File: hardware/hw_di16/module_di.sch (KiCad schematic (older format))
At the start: 142 parts, among them P1 DEBUG, P2 DI_0, P3 DI_1, P4 MOD_IN, U1 STM32F103C8Tx, U2 TLP291-4, U3 TLP291-4, U4 TLP291-4, U5 TLP291-4

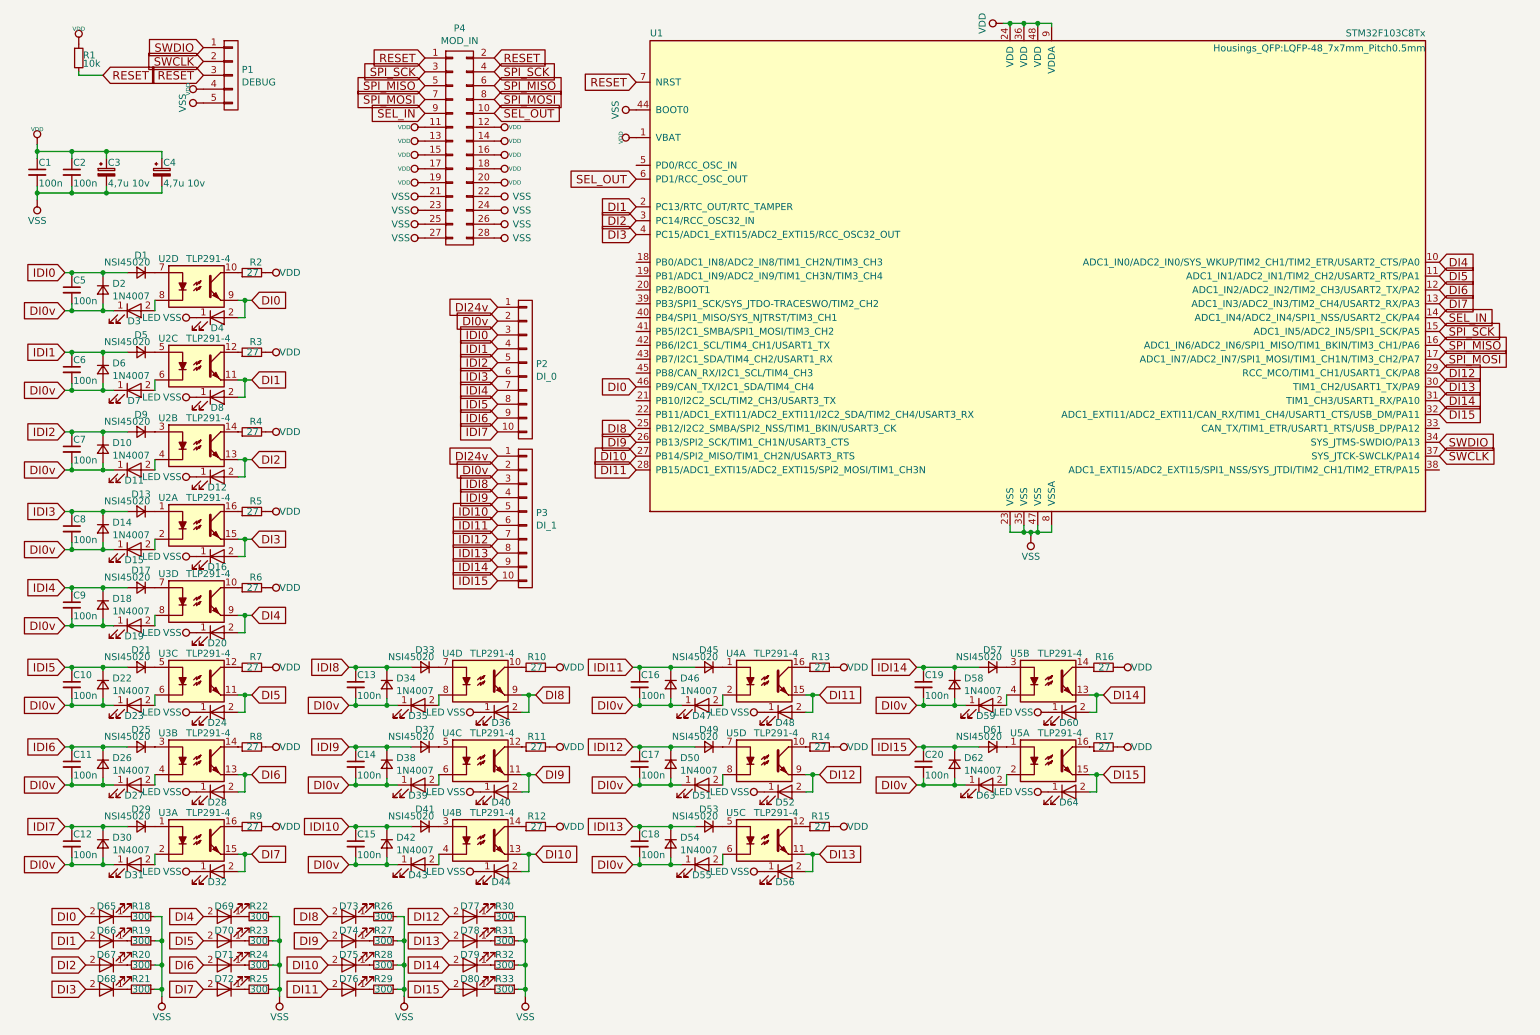
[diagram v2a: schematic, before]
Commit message: Обновлена плата DI16.
Завершена предварительная разводка.
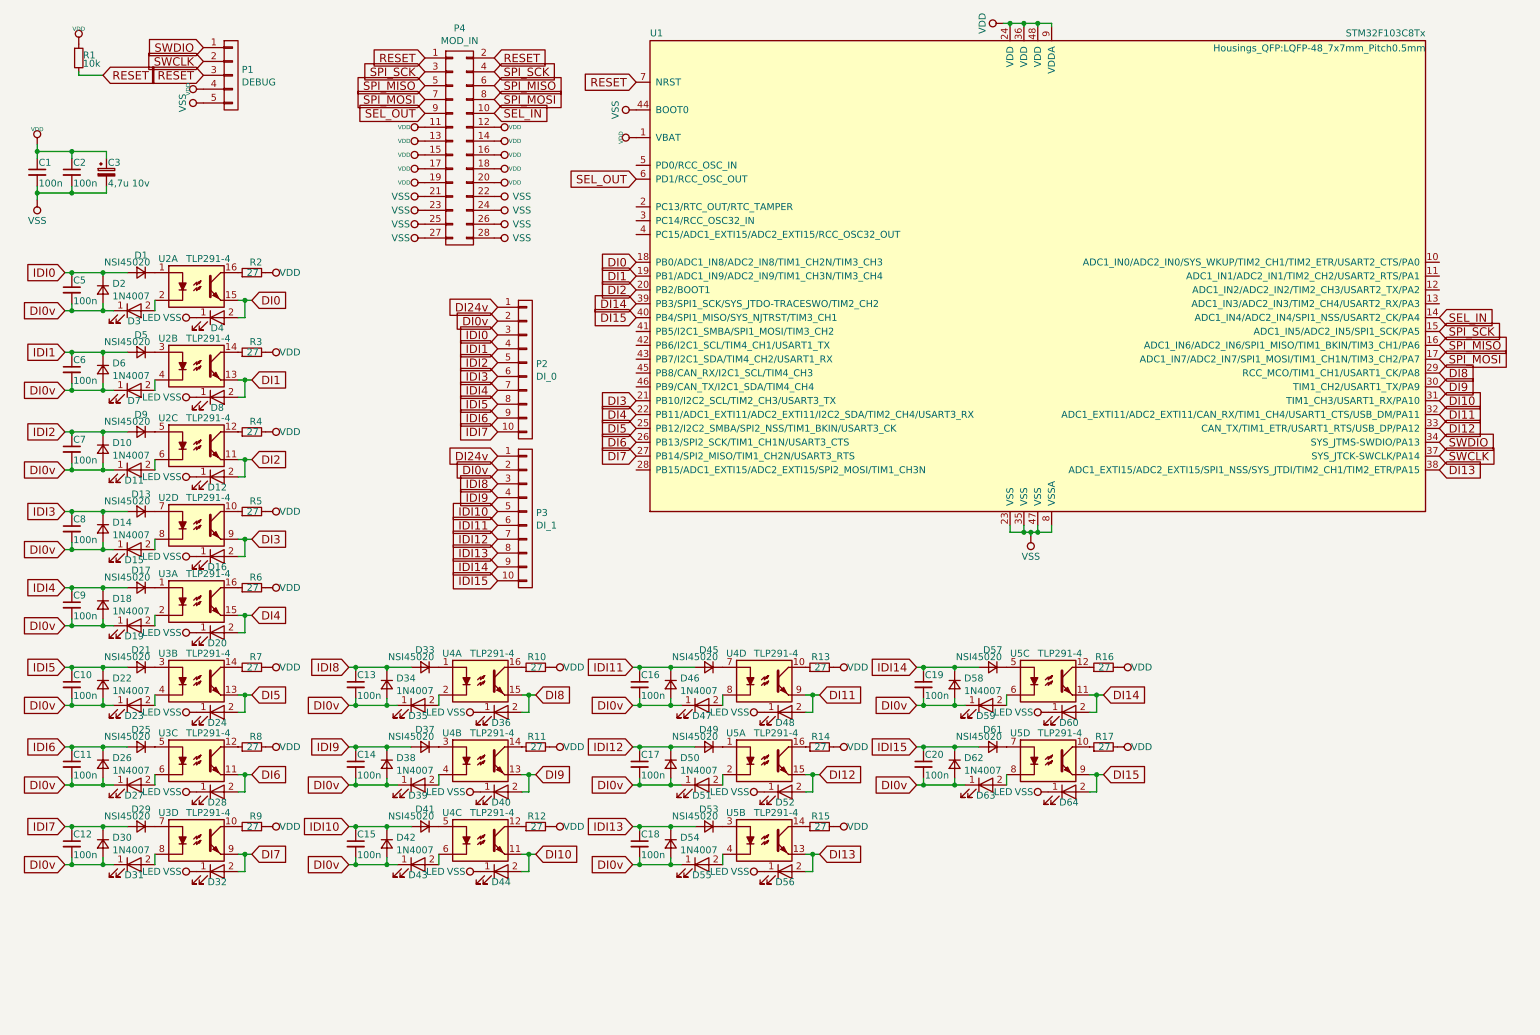
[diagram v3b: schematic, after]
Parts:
- removed C4: 4,7u 10v, Capacitors_Tantalum_SMD:CP_Tantalum_Case-A_EIA-3216-18_Reflow, symbol CP_Small
- removed D65, D66, D67, D68, D69, D70, D71, D72, D73, D74, D75, D76, D77, D78, D79, D80: LED, LEDs:LED_0805, symbol LED
- removed R18, R19, R20, R21, R22, R23, R24, R25, R26, R27, R28, R29, R30, R31, R32, R33: 300, Resistors_SMD:R_0805, symbol R_Small
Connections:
- net DI0: now also U1.18 (PB0/ADC1_IN8/ADC2_IN8/TIM1_CH2N/TIM3_CH3), U2.15; no longer U1.46 (PB9/CAN_TX/I2C1_SDA/TIM4_CH4), U2.9
- net DI1: now also U1.19 (PB1/ADC1_IN9/ADC2_IN9/TIM1_CH3N/TIM3_CH4), U2.13; no longer U1.2 (PC13/RTC_OUT/RTC_TAMPER), U2.11
- net DI10: now also U1.31 (TIM1_CH3/USART1_RX/PA10), U4.11; no longer U1.27 (PB14/SPI2_MISO/TIM1_CH2N/USART3_RTS), U4.13
- net DI11: now also U1.32 (ADC1_EXTI11/ADC2_EXTI11/CAN_RX/TIM1_CH4/USART1_CTS/USB_DM/PA11), U4.9; no longer U1.28 (PB15/ADC1_EXTI15/ADC2_EXTI15/SPI2_MOSI/TIM1_CH3N), U4.15
- net DI12: now also U1.33 (CAN_TX/TIM1_ETR/USART1_RTS/USB_DP/PA12), U5.15; no longer U1.29 (RCC_MCO/TIM1_CH1/USART1_CK/PA8), U5.9
- net DI13: now also U1.38 (ADC1_EXTI15/ADC2_EXTI15/SPI1_NSS/SYS_JTDI/TIM2_CH1/TIM2_ETR/PA15), U5.13; no longer U1.30 (TIM1_CH2/USART1_TX/PA9), U5.11
- net DI14: now also U1.39 (PB3/SPI1_SCK/SYS_JTDO-TRACESWO/TIM2_CH2), U5.11; no longer U1.31 (TIM1_CH3/USART1_RX/PA10), U5.13
- net DI15: now also U1.40 (PB4/SPI1_MISO/SYS_NJTRST/TIM3_CH1), U5.9; no longer U1.32 (ADC1_EXTI11/ADC2_EXTI11/CAN_RX/TIM1_CH4/USART1_CTS/USB_DM/PA11), U5.15
- net DI2: now also U1.20 (PB2/BOOT1), U2.11; no longer U1.3 (PC14/RCC_OSC32_IN), U2.13
- net DI3: now also U1.21 (PB10/I2C2_SCL/TIM2_CH3/USART3_TX), U2.9; no longer U1.4 (PC15/ADC1_EXTI15/ADC2_EXTI15/RCC_OSC32_OUT), U2.15
- net DI4: now also U1.22 (PB11/ADC1_EXTI11/ADC2_EXTI11/I2C2_SDA/TIM2_CH4/USART3_RX), U3.15; no longer U1.10 (ADC1_IN0/ADC2_IN0/SYS_WKUP/TIM2_CH1/TIM2_ETR/USART2_CTS/PA0), U3.9
- net DI5: now also U1.25 (PB12/I2C2_SMBA/SPI2_NSS/TIM1_BKIN/USART3_CK), U3.13; no longer U1.11 (ADC1_IN1/ADC2_IN1/TIM2_CH2/USART2_RTS/PA1), U3.11
- net DI6: now also U1.26 (PB13/SPI2_SCK/TIM1_CH1N/USART3_CTS), U3.11; no longer U1.12 (ADC1_IN2/ADC2_IN2/TIM2_CH3/USART2_TX/PA2), U3.13
- net DI7: now also U1.27 (PB14/SPI2_MISO/TIM1_CH2N/USART3_RTS), U3.9; no longer U1.13 (ADC1_IN3/ADC2_IN3/TIM2_CH4/USART2_RX/PA3), U3.15
- net DI8: now also U1.29 (RCC_MCO/TIM1_CH1/USART1_CK/PA8), U4.15; no longer U1.25 (PB12/I2C2_SMBA/SPI2_NSS/TIM1_BKIN/USART3_CK), U4.9
- net DI9: now also U1.30 (TIM1_CH2/USART1_TX/PA9), U4.13; no longer U1.26 (PB13/SPI2_SCK/TIM1_CH1N/USART3_CTS), U4.11
- net SEL_IN: now also P4.10 (P10); no longer P4.9 (P9)
- net SEL_OUT: now also P4.9 (P9); no longer P4.10 (P10)
- net at R2.1: now also U2.16; no longer U2.10
- net at D1.1 (K): now also U2.1; no longer U2.7
- net at D3.2 (A): now also U2.2; no longer U2.8
- net at R3.1: now also U2.14; no longer U2.12
- net at D5.1 (K): now also U2.3; no longer U2.5
- net at D7.2 (A): now also U2.4; no longer U2.6
- net at R4.1: now also U2.12; no longer U2.14
- net at D9.1 (K): now also U2.5; no longer U2.3
- net at D11.2 (A): now also U2.6; no longer U2.4
- net at D13.1 (K): now also U2.7; no longer U2.1
- net at R5.1: now also U2.10; no longer U2.16
- net at D15.2 (A): now also U2.8; no longer U2.2
- net at R6.1: now also U3.16; no longer U3.10
- net at D17.1 (K): now also U3.1; no longer U3.7
- net at D19.2 (A): now also U3.2; no longer U3.8
- net at R7.1: now also U3.14; no longer U3.12
- net at D21.1 (K): now also U3.3; no longer U3.5
- net at D23.2 (A): now also U3.4; no longer U3.6
- net at R8.1: now also U3.12; no longer U3.14
- net at D25.1 (K): now also U3.5; no longer U3.3
- net at D27.2 (A): now also U3.6; no longer U3.4
- net at D29.1 (K): now also U3.7; no longer U3.1
- net at R9.1: now also U3.10; no longer U3.16
- net at D31.2 (A): now also U3.8; no longer U3.2
- net at R10.1: now also U4.16; no longer U4.10
- net at D33.1 (K): now also U4.1; no longer U4.7
- net at D35.2 (A): now also U4.2; no longer U4.8
- net at R11.1: now also U4.14; no longer U4.12
- net at D37.1 (K): now also U4.3; no longer U4.5
- net at D39.2 (A): now also U4.4; no longer U4.6
- net at R12.1: now also U4.12; no longer U4.14
- net at D41.1 (K): now also U4.5; no longer U4.3
- net at D43.2 (A): now also U4.6; no longer U4.4
- net at D45.1 (K): now also U4.7; no longer U4.1
- net at R13.1: now also U4.10; no longer U4.16
- net at D47.2 (A): now also U4.8; no longer U4.2
- net at R14.1: now also U5.16; no longer U5.10
- net at D49.1 (K): now also U5.1; no longer U5.7
- net at D51.2 (A): now also U5.2; no longer U5.8
- net at R15.1: now also U5.14; no longer U5.12
- net at D53.1 (K): now also U5.3; no longer U5.5
- net at D55.2 (A): now also U5.4; no longer U5.6
- net at R16.1: now also U5.12; no longer U5.14
- net at D57.1 (K): now also U5.5; no longer U5.3
- net at D59.2 (A): now also U5.6; no longer U5.4
- net at D61.1 (K): now also U5.7; no longer U5.1
- net at R17.1: now also U5.10; no longer U5.16
- net at D63.2 (A): now also U5.8; no longer U5.2

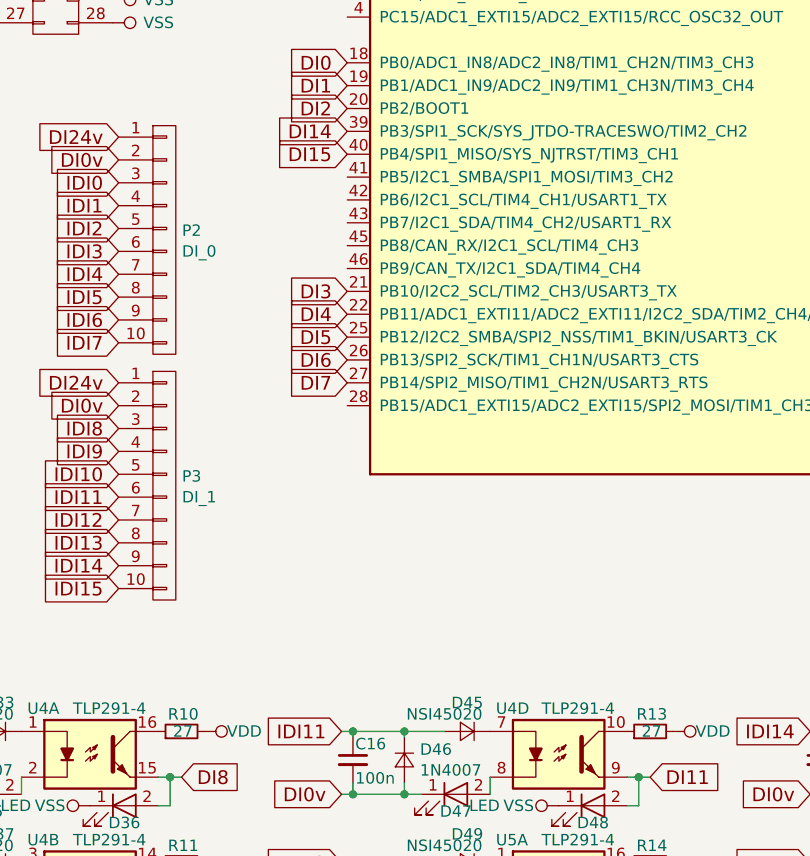
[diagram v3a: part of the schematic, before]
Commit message: Обновлена плата модуля DI16.
Добавлены статусные светодиоды.
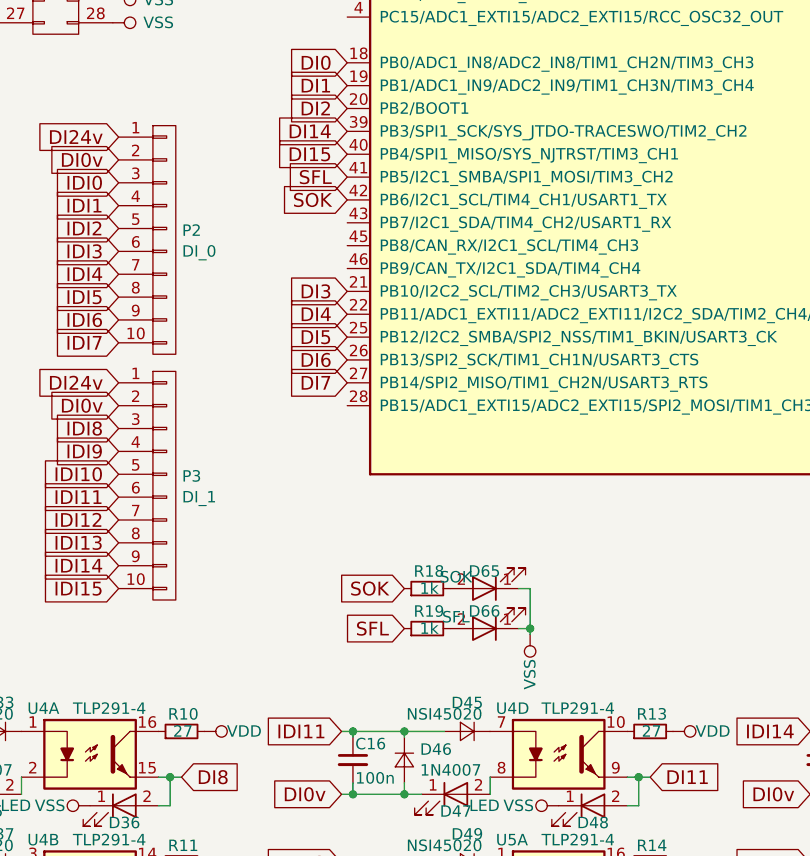
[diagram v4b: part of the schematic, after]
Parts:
- added D65: SOK, LEDs:LED_0805, symbol LED
- added D66: SFL, LEDs:LED_0805, symbol LED
- added R18, R19: 1k, Resistors_SMD:R_0805, symbol R_Small
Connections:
- net VSS: now also D65.1 (K), D66.1 (K)
- net SFL: now reaches U1.41 (PB5/I2C1_SMBA/SPI1_MOSI/TIM3_CH2)
- net SFL: now also R19.1
- net SOK: now reaches U1.42 (PB6/I2C1_SCL/TIM4_CH1/USART1_TX)
- net SOK: now also R18.1
- new net: D65.2 (A), R18.2
- new net: D66.2 (A), R19.2

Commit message: Обновлена шелкография на платах.
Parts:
- D11, D12, D15, D16, D19, D20, D23, D24, D27, D28, D3, D31, D32, D35, D36, D39, D4, D40, D43, D44, D47, D48, D51, D52, D55, D56, D59, D60, D63, D64, D65, D66, D7, D8: footprint LEDs:LED_0805 -> LEDs:LED_0603

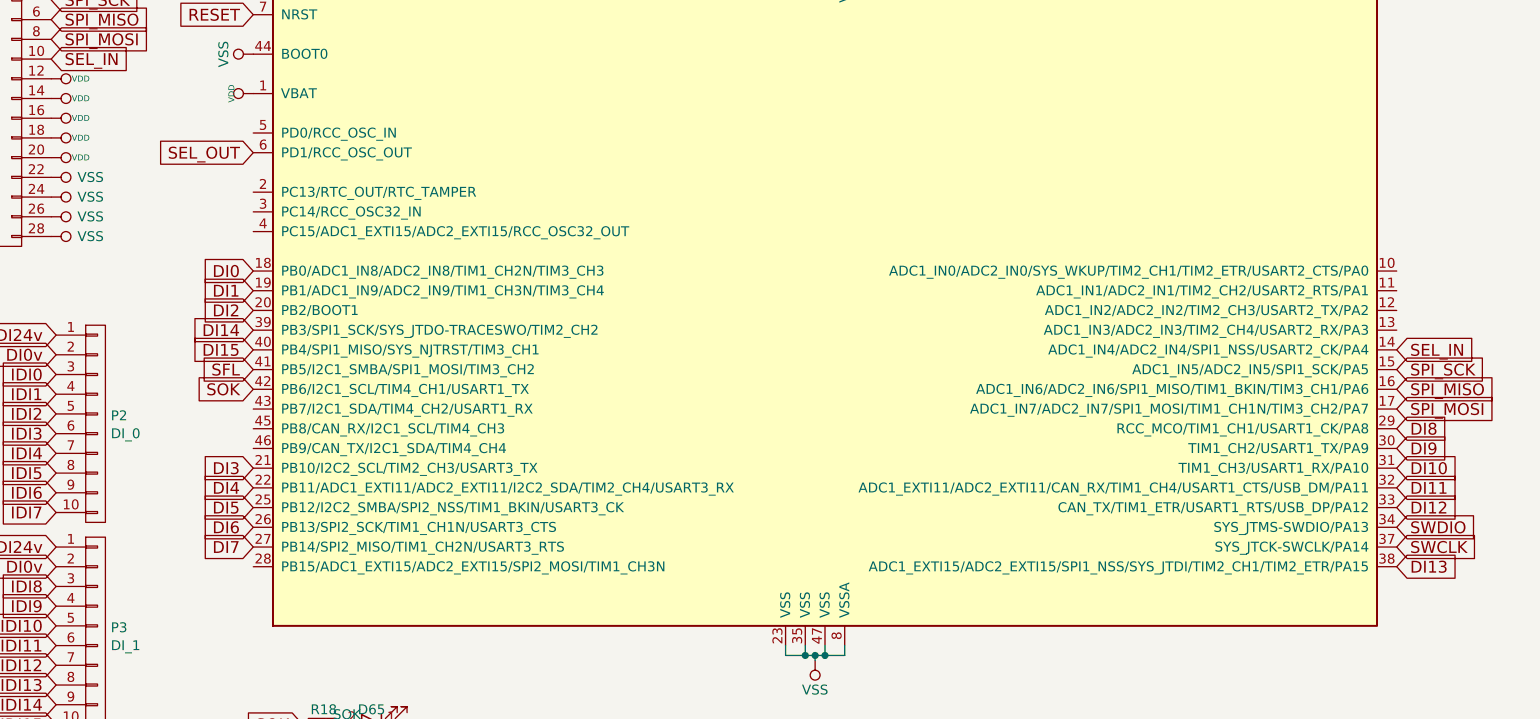
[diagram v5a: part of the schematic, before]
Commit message: Обновлены платы модулей - приведены к единому виду.
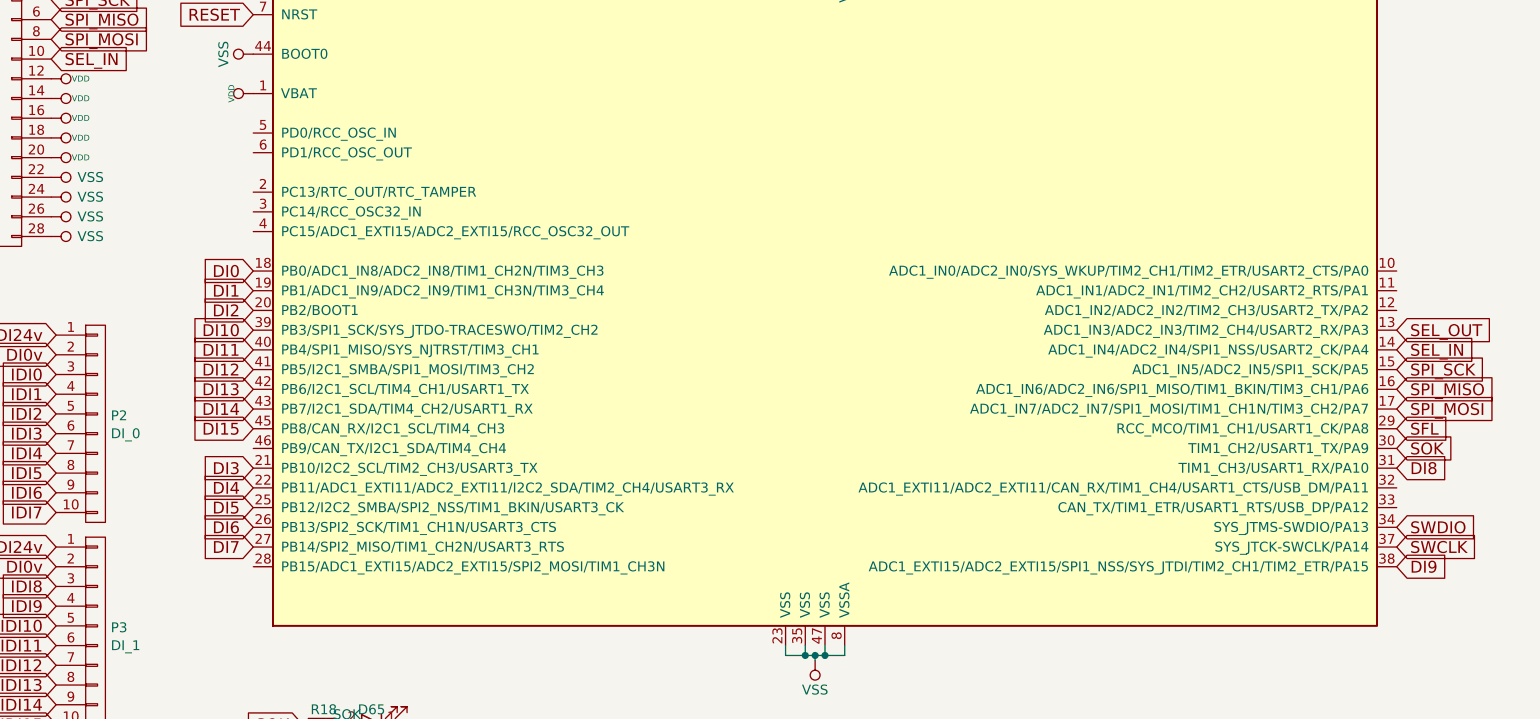
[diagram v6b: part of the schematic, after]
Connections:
- net DI10: now also U1.39 (PB3/SPI1_SCK/SYS_JTDO-TRACESWO/TIM2_CH2); no longer U1.31 (TIM1_CH3/USART1_RX/PA10)
- net DI11: now also U1.40 (PB4/SPI1_MISO/SYS_NJTRST/TIM3_CH1); no longer U1.32 (ADC1_EXTI11/ADC2_EXTI11/CAN_RX/TIM1_CH4/USART1_CTS/USB_DM/PA11)
- net DI12: now also U1.41 (PB5/I2C1_SMBA/SPI1_MOSI/TIM3_CH2); no longer U1.33 (CAN_TX/TIM1_ETR/USART1_RTS/USB_DP/PA12)
- net DI13: now also U1.42 (PB6/I2C1_SCL/TIM4_CH1/USART1_TX); no longer U1.38 (ADC1_EXTI15/ADC2_EXTI15/SPI1_NSS/SYS_JTDI/TIM2_CH1/TIM2_ETR/PA15)
- net DI14: now also U1.43 (PB7/I2C1_SDA/TIM4_CH2/USART1_RX); no longer U1.39 (PB3/SPI1_SCK/SYS_JTDO-TRACESWO/TIM2_CH2)
- net DI15: now also U1.45 (PB8/CAN_RX/I2C1_SCL/TIM4_CH3); no longer U1.40 (PB4/SPI1_MISO/SYS_NJTRST/TIM3_CH1)
- net DI8: now also U1.31 (TIM1_CH3/USART1_RX/PA10); no longer U1.29 (RCC_MCO/TIM1_CH1/USART1_CK/PA8)
- net DI9: now also U1.38 (ADC1_EXTI15/ADC2_EXTI15/SPI1_NSS/SYS_JTDI/TIM2_CH1/TIM2_ETR/PA15); no longer U1.30 (TIM1_CH2/USART1_TX/PA9)
- net SEL_OUT: now also U1.13 (ADC1_IN3/ADC2_IN3/TIM2_CH4/USART2_RX/PA3); no longer U1.6 (PD1/RCC_OSC_OUT)
- net SFL: now also U1.29 (RCC_MCO/TIM1_CH1/USART1_CK/PA8); no longer U1.41 (PB5/I2C1_SMBA/SPI1_MOSI/TIM3_CH2)
- net SOK: now also U1.30 (TIM1_CH2/USART1_TX/PA9); no longer U1.42 (PB6/I2C1_SCL/TIM4_CH1/USART1_TX)
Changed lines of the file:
@@
 LIBS:powerint
 LIBS:module_di-cache
-EELAYER 25 0
+EELAYER 26 0
 EELAYER END
 $Descr A4 11693 8268
@@
 Comment4 ""
 $EndDescr
-Text GLabel 4925 2650 0    60   Input ~ 0
+Text GLabel 4925 3050 0    60   Input ~ 0
 DI15
-Text GLabel 4925 2550 0    60   Input ~ 0
+Text GLabel 4925 2950 0    60   Input ~ 0
 DI14
 Text GLabel 4925 2250 0    60   Input ~ 0
@@
 Text GLabel 4925 3450 0    60   Input ~ 0
 DI5
+Text GLabel 4925 2850 0    60   Input ~ 0
+DI13
+Text GLabel 4925 2750 0    60   Input ~ 0
+DI12
+Text GLabel 4925 2650 0    60   Input ~ 0
+DI11
 Text GLabel 10725 3750 2    60   Input ~ 0
-DI13
-Text GLabel 10725 3450 2    60   Input ~ 0
-DI12
-Text GLabel 10725 3350 2    60   Input ~ 0
-DI11
-Text GLabel 10725 3150 2    60   Input ~ 0
 DI9
-Text GLabel 10725 3250 2    60   Input ~ 0
+Text GLabel 4925 2550 0    60   Input ~ 0
 DI10
 Text GLabel 10725 3650 2    60   Input ~ 0
@@
 Text GLabel 4925 3650 0    60   Input ~ 0
 DI7
-Text GLabel 10725 3050 2    60   Input ~ 0
+Text GLabel 10725 3250 2    60   Input ~ 0
 DI8
 Text GLabel 3925 2775 0    60   Input ~ 0
@@
 Text GLabel 10725 2650 2    60   Input ~ 0
 SEL_IN
-Text GLabel 4925 1650 0    60   Input ~ 0
+Text GLabel 10725 2550 2    60   Input ~ 0
 SEL_OUT
 Text GLabel 1800 700  0    60   Input ~ 0
@@
 Text GLabel 5175 4725 0    60   Input ~ 0
 SFL
-Text GLabel 4925 2750 0    60   Input ~ 0
+Text GLabel 10725 3050 2    60   Input ~ 0
 SFL
-Text GLabel 4925 2850 0    60   Input ~ 0
+Text GLabel 10725 3150 2    60   Input ~ 0
 SOK
 $EndSCHEMATC
